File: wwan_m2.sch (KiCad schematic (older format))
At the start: 45 parts, among them J7 SIM_Card_Det, J8 SIM_Card_Det, J9 MDT180B03001, SW8 WWAN_HKS, U17 NTS0102GT, U18 NUP5120, U19 NUP5120, U20 NTB0104GU12

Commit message: Begin creating the IMX8M-SOM schematic symbol, remove the old DART-MX8M symbol
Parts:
- renumbered C61 to C75, C62 to C76, C63 to C77, C64 to C78, C65 to C79, C66 to C80, C67 to C81, C68 to C82, C69 to C83, C70 to C84, C71 to C85, C72 to C86, C73 to C87, C74 to C88, C75 to C89, C76 to C90, C77 to C91, C78 to C92, C79 to C93, C80 to C94, C81 to C95, C82 to C96, C83 to C97, D17 to D19, D18 to D20, D19 to D21, J9 to J10, J7 to J8, J8 to J9, R76 to R81, R77 to R82, R78 to R83, R79 to R84, R80 to R85, R81 to R86, R82 to R87, R83 to R88, R84 to R89, R85 to R90, R86 to R91, U17 to U18, U18 to U19, U19 to U20, U20 to U21

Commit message: Assign all associated signals to their respective pins on the EmCraft i.MX8M SoM
The ERC is now at the same state as the DART SoM schematic. Need to compare various aspects of the current schematic against the EmCraft reference design. The main buck-boost will likely need to be switched to a 5V regulator, or be configured to output 5V.

A regulator will likely need to be added which will output some VBAT voltage level (3.5~4.2V) for the M.2 cards. The SIM7100 for example requires at least 3.4V!
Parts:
- renumbered C97 to C100, C75 to C78, C76 to C79, C77 to C80, C78 to C81, C79 to C82, C80 to C83, C81 to C84, C82 to C85, C83 to C86, C84 to C87, C85 to C88, C86 to C89, C87 to C90, C88 to C91, C89 to C92, C90 to C93, C91 to C94, C92 to C95, C93 to C96, C94 to C97, C95 to C98, C96 to C99

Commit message: Use "Start to sheet number*100 and use first free number" designation, any new component added to the schematic will occupy the next available number in that sheet
For example: if sheet 2 has R201-R215 and we add a new resistor it will become R216.
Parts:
- renumbered C78 to C1401, C79 to C1402, C80 to C1403, C81 to C1404, C82 to C1405, C83 to C1406, C84 to C1407, C85 to C1408, C86 to C1409, C87 to C1410, C88 to C1411, C89 to C1412, C90 to C1413, C91 to C1414, C92 to C1415, C93 to C1416, C94 to C1417, C95 to C1418, C96 to C1419, C97 to C1420, C98 to C1421, C99 to C1422, C100 to C1423, D19 to D1401, D20 to D1402, D21 to D1403, J8 to J1401, J9 to J1402, J10 to J1403, R81 to R1401, R82 to R1402, R83 to R1403, R84 to R1404, R85 to R1405, R86 to R1406, R87 to R1407, R88 to R1408, R89 to R1409, R90 to R1410, R91 to R1411, SW8 to SW1401, U18 to U1401, U19 to U1402, U20 to U1403, U21 to U1404

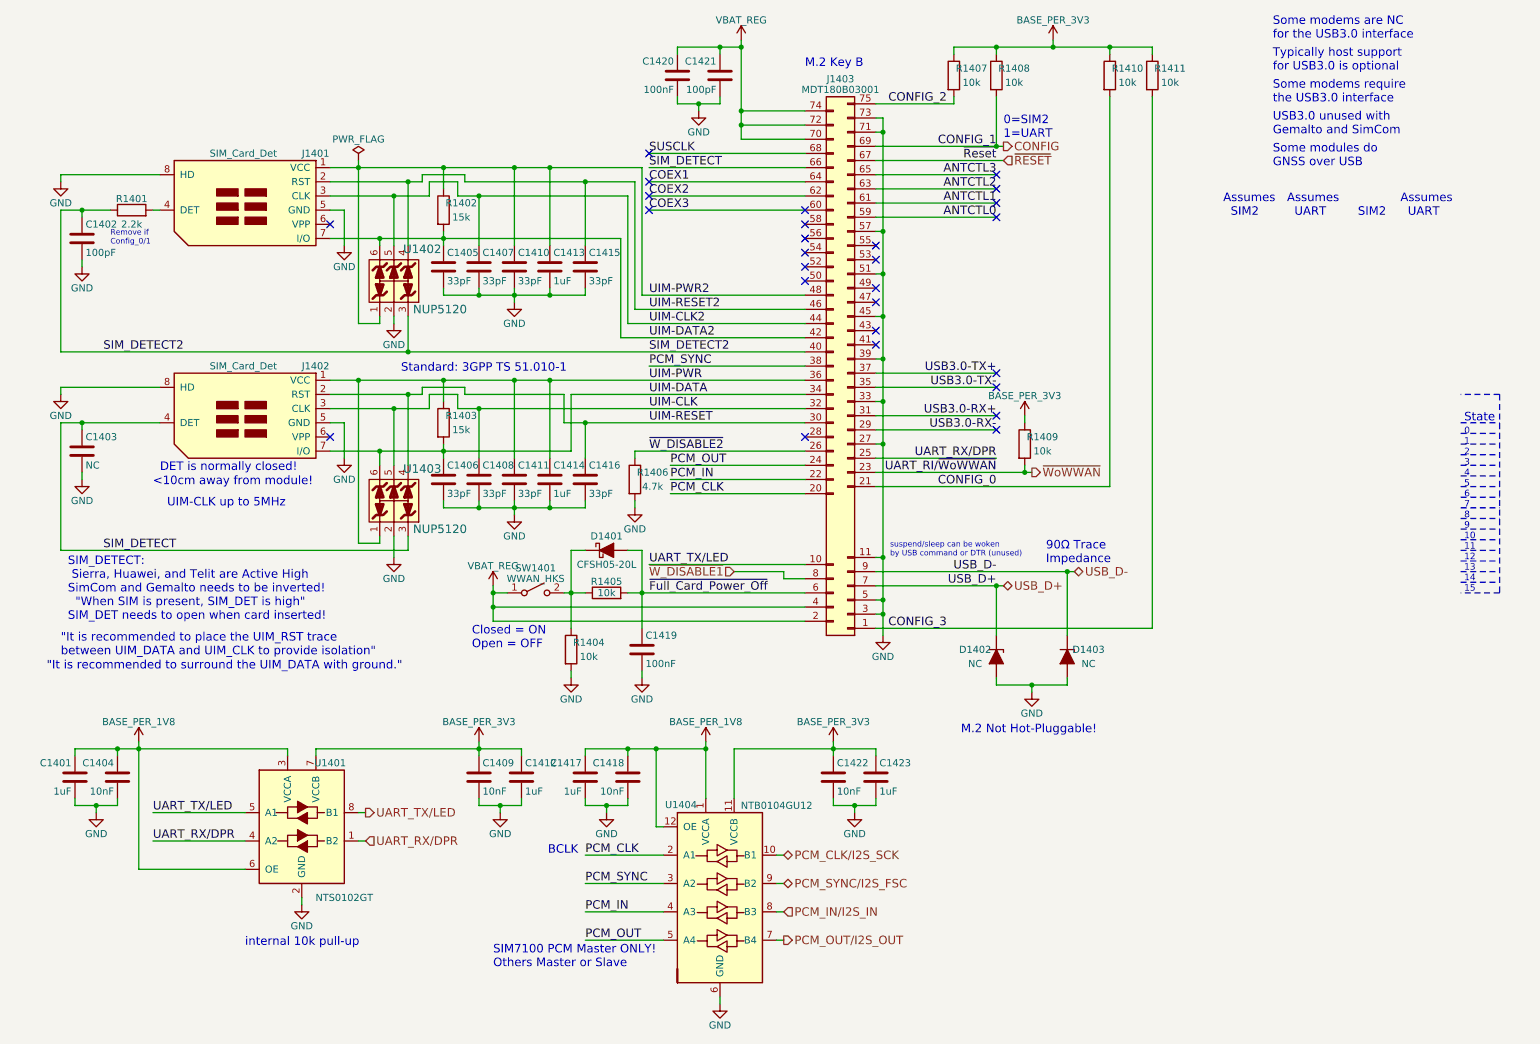
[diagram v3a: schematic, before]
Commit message: Move reference designators in the schematic so that they are legible
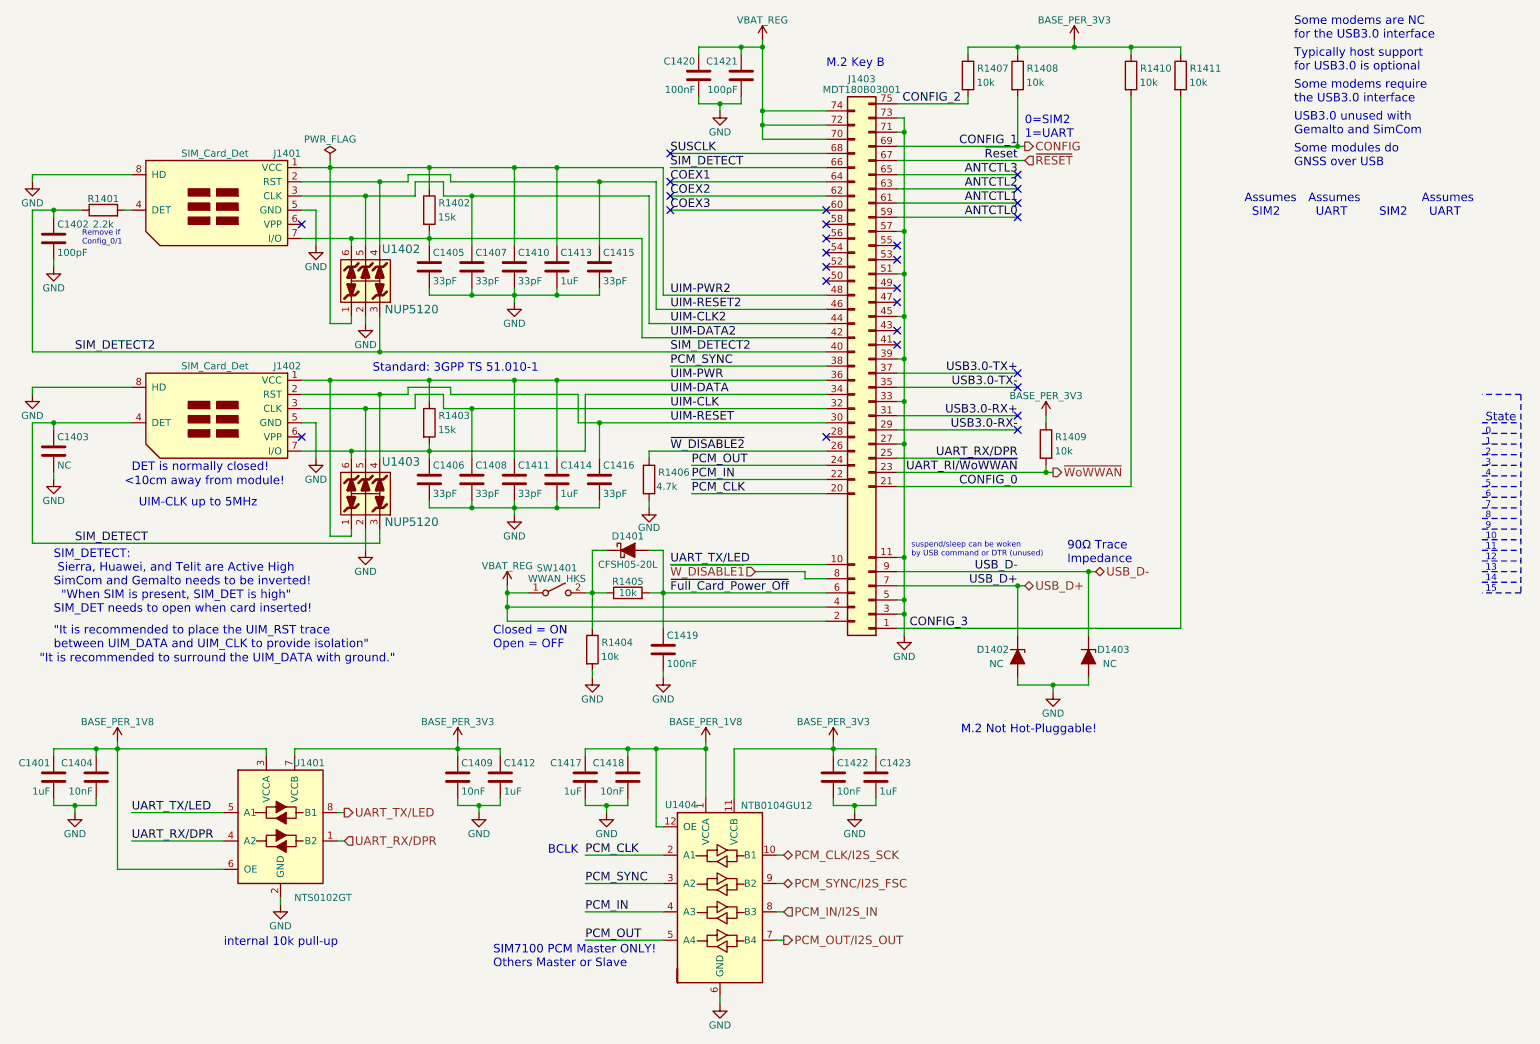
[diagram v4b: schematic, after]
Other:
- moved on the sheet: C1401, C1402, C1403, C1404, C1405, C1406, C1407, C1408, C1409, C1412, C1413, C1414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

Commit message: Include reverse polarity protection circuit along with a simulation showing its effectiveness
Protecting VBAT from when board is sinking current via USB C. Protects against reverse polarity at the DC jack.

In EmCraft's instance VBUS should only be 5V when sinking current but they must protect against the condition when VBUS>12V and DC_IN=12V. This may need testing.
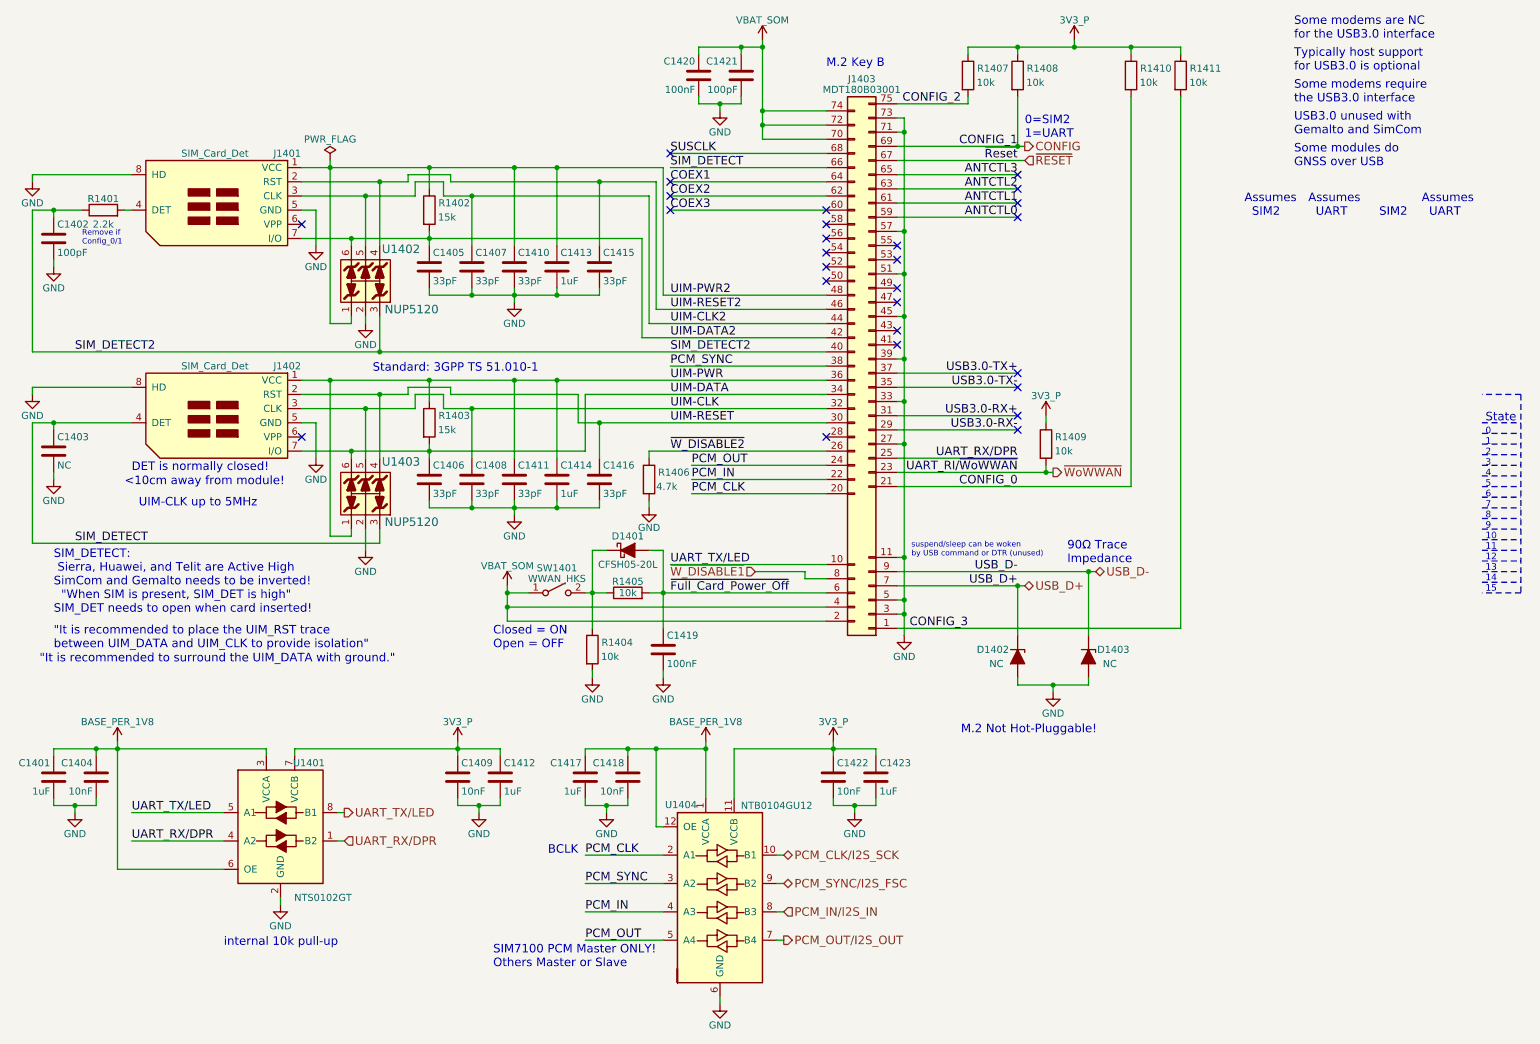
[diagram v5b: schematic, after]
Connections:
- net BASE_PER_3V3 renamed 3V3_P
- net VBAT_REG renamed VBAT_SOM

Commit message: Stick the WWAM M.2 sheet above/before the audio sheet
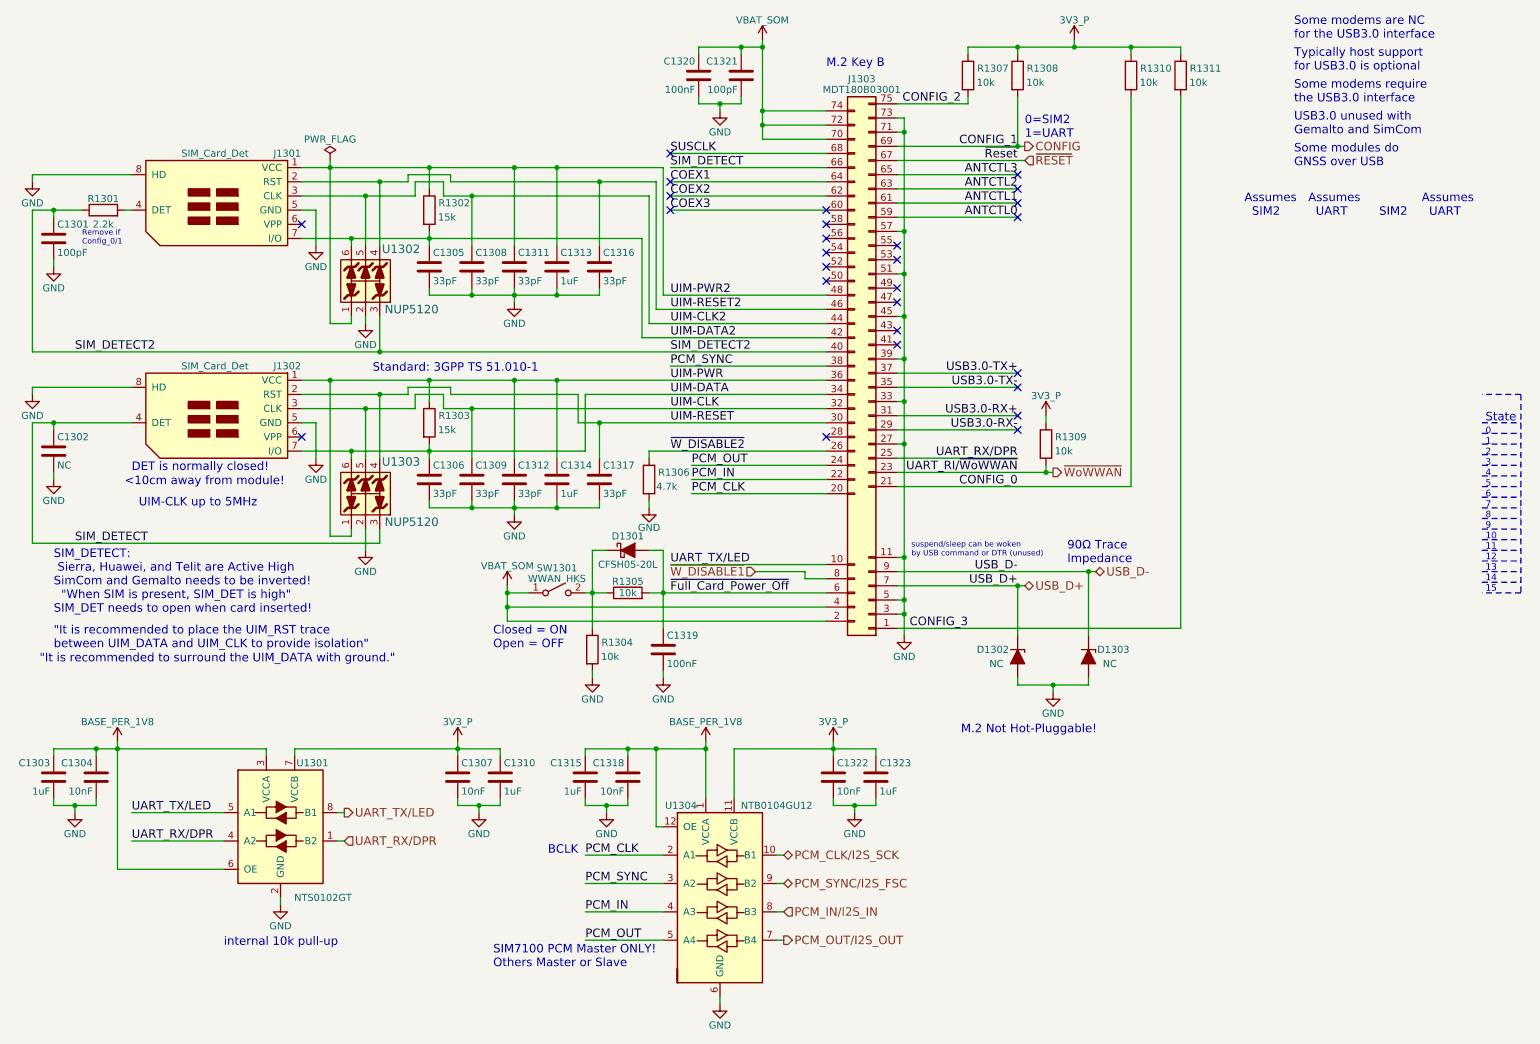
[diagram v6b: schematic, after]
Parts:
- renumbered C1402 to C1301, C1403 to C1302, C1401 to C1303, C1404 to C1304, C1405 to C1305, C1406 to C1306, C1409 to C1307, C1407 to C1308, C1408 to C1309, C1412 to C1310, C1410 to C1311, C1411 to C1312, C1413 to C1313, C1414 to C1314, C1417 to C1315, C1415 to C1316, C1416 to C1317, C1418 to C1318, C1419 to C1319, C1420 to C1320, C1421 to C1321, C1422 to C1322, C1423 to C1323, D1401 to D1301, D1402 to D1302, D1403 to D1303, J1401 to J1301, J1402 to J1302, J1403 to J1303, R1401 to R1301, R1402 to R1302, R1403 to R1303, R1404 to R1304, R1405 to R1305, R1406 to R1306, R1407 to R1307, R1408 to R1308, R1409 to R1309, R1410 to R1310, R1411 to R1311, SW1401 to SW1301, U1401 to U1301, U1402 to U1302, U1403 to U1303, U1404 to U1304

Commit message: Add USB type C circuit with DRP PD capability, should sink near 2A @ 5-6.5V and source 550mA @ 5V
Removed the reverse current protection circuit from the last commit due to the requirement changing to only 18650 battery and USB-C being possible power sources

Next thing to add is the charging circuit when the USB-C is in sink mode/role
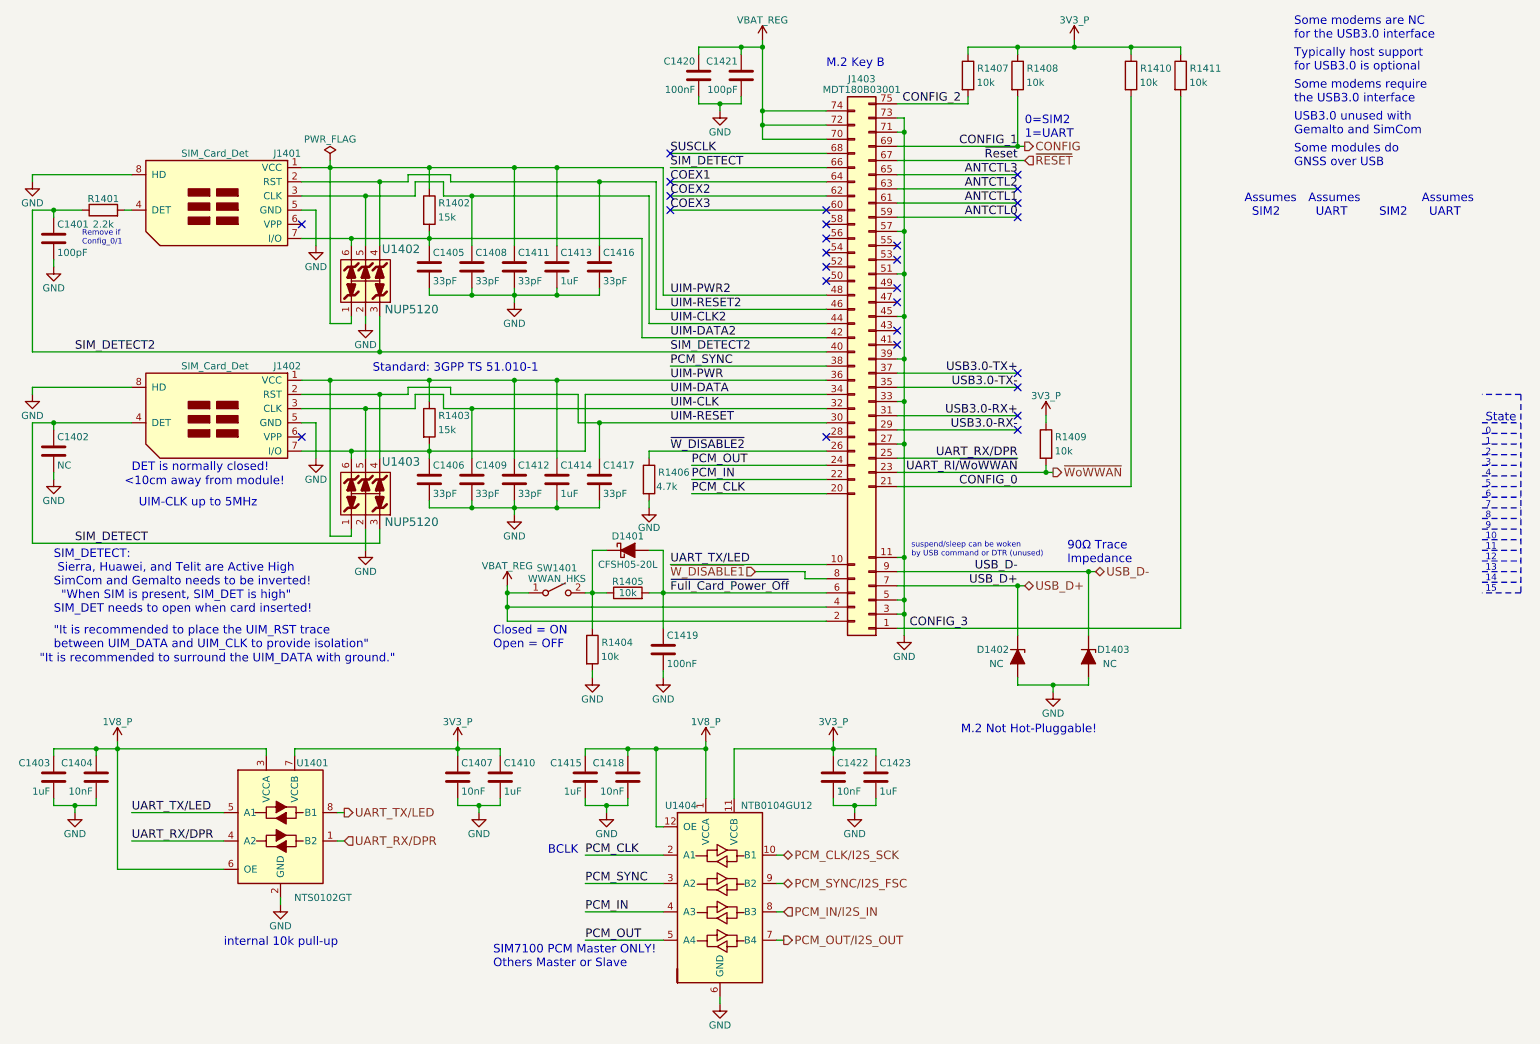
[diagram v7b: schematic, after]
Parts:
- renumbered C1301 to C1401, C1302 to C1402, C1303 to C1403, C1304 to C1404, C1305 to C1405, C1306 to C1406, C1307 to C1407, C1308 to C1408, C1309 to C1409, C1310 to C1410, C1311 to C1411, C1312 to C1412, C1313 to C1413, C1314 to C1414, C1315 to C1415, C1316 to C1416, C1317 to C1417, C1318 to C1418, C1319 to C1419, C1320 to C1420, C1321 to C1421, C1322 to C1422, C1323 to C1423, D1301 to D1401, D1302 to D1402, D1303 to D1403, J1301 to J1401, J1302 to J1402, J1303 to J1403, R1301 to R1401, R1302 to R1402, R1303 to R1403, R1304 to R1404, R1305 to R1405, R1306 to R1406, R1307 to R1407, R1308 to R1408, R1309 to R1409, R1310 to R1410, R1311 to R1411, SW1301 to SW1401, U1301 to U1401, U1302 to U1402, U1303 to U1403, U1304 to U1404
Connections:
- net BASE_PER_1V8 renamed 1V8_P
- net VBAT_SOM renamed VBAT_REG
